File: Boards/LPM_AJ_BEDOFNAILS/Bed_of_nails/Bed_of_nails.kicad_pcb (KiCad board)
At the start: 2 copper layers, 130 x 90 mm, 66 parts, among them J1 TU, J10 TU1, J11 TU2, J12 TU3, J13 TU4, J2 TD, J3 V+RS485, J4 PT, J5 Conn_ZIF_9, J6 TD1, J7 TD2, J8 TD3, J9 TD4, U1 Conn_ZIF_5pos

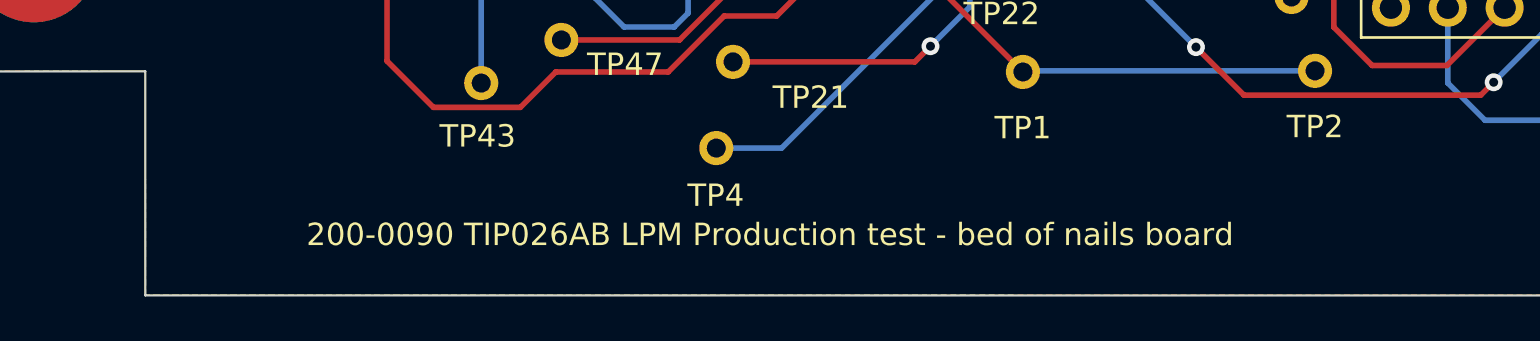
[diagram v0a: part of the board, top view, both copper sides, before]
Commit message: Figuring out why supply cal not working
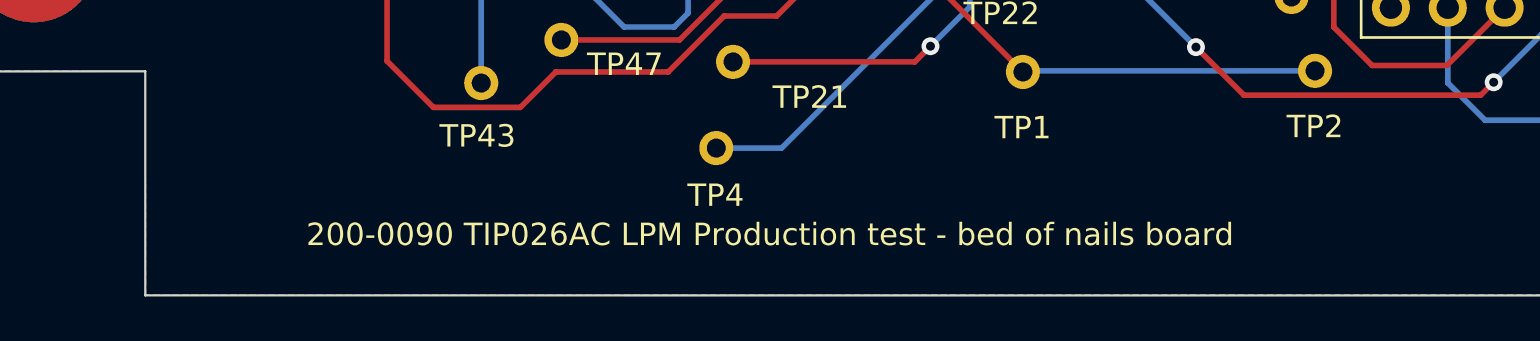
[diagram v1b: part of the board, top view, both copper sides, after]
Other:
- board text added: "200-0090 TIP026AC LPM Production test - bed of nails board"
- board text removed: "200-0090 TIP026AB LPM Production test - bed of nails board"
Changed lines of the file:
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@@
     (effects (font (size 1 1) (thickness 0.15)))
   )
-  (gr_text "200-0090 TIP026AB LPM Production test - bed of nails board" (at 130.88 133.12) (layer "F.SilkS")
+  (gr_text "200-0090 TIP026AC LPM Production test - bed of nails board" (at 130.88 133.12) (layer "F.SilkS")
     (effects (font (size 1 1) (thickness 0.15)))
   )

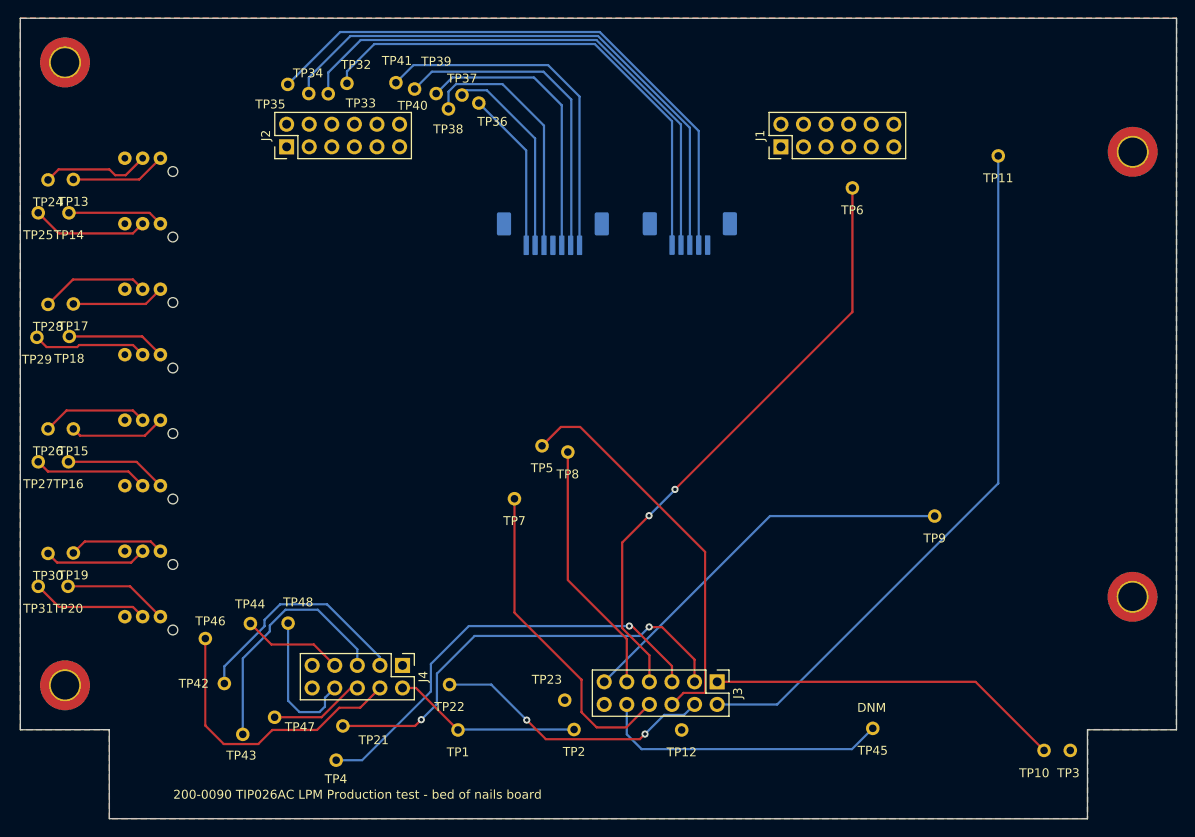
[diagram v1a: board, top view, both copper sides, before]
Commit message: added relay
Still needs better separation between the AC lines and footprints relay need fixing
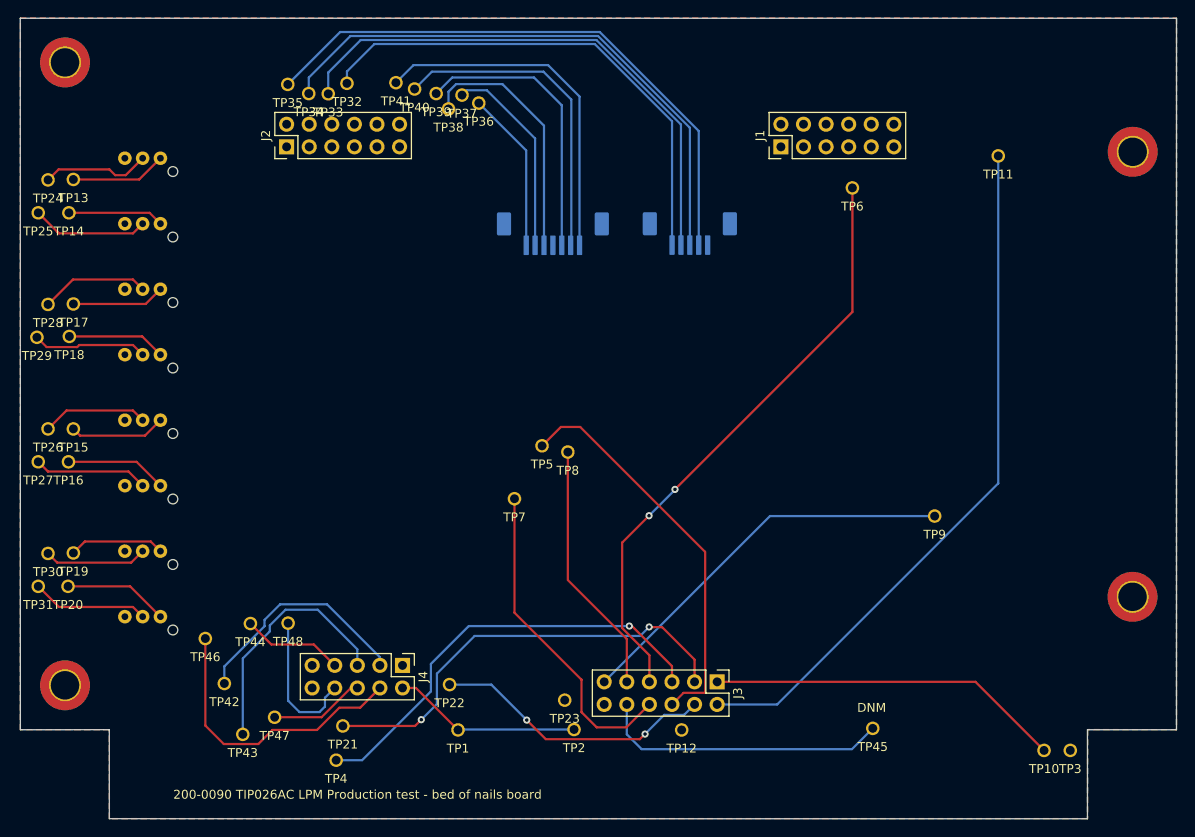
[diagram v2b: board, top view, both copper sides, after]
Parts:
- TP1, TP10, TP11, TP12, TP13, TP14, TP15, TP16, TP17, TP18, TP19, TP2, TP20, TP21, TP22, TP23, TP24, TP25, TP26, TP27, TP28, TP29, TP3, TP30, TP31, TP32, TP33, TP34, TP35, TP36, TP37, TP38, TP39, TP4, TP40, TP41, TP42, TP43, TP44, TP45, TP46, TP47, TP48, TP5, TP6, TP7, TP8, TP9: footprint MyFootprints:KS-075-47-G-10_KS-07547G10 -> MyFootPrints:INGUN_KS-075-47-G-10_KS-07547G10
